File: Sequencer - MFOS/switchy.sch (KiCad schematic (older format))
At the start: 52 parts

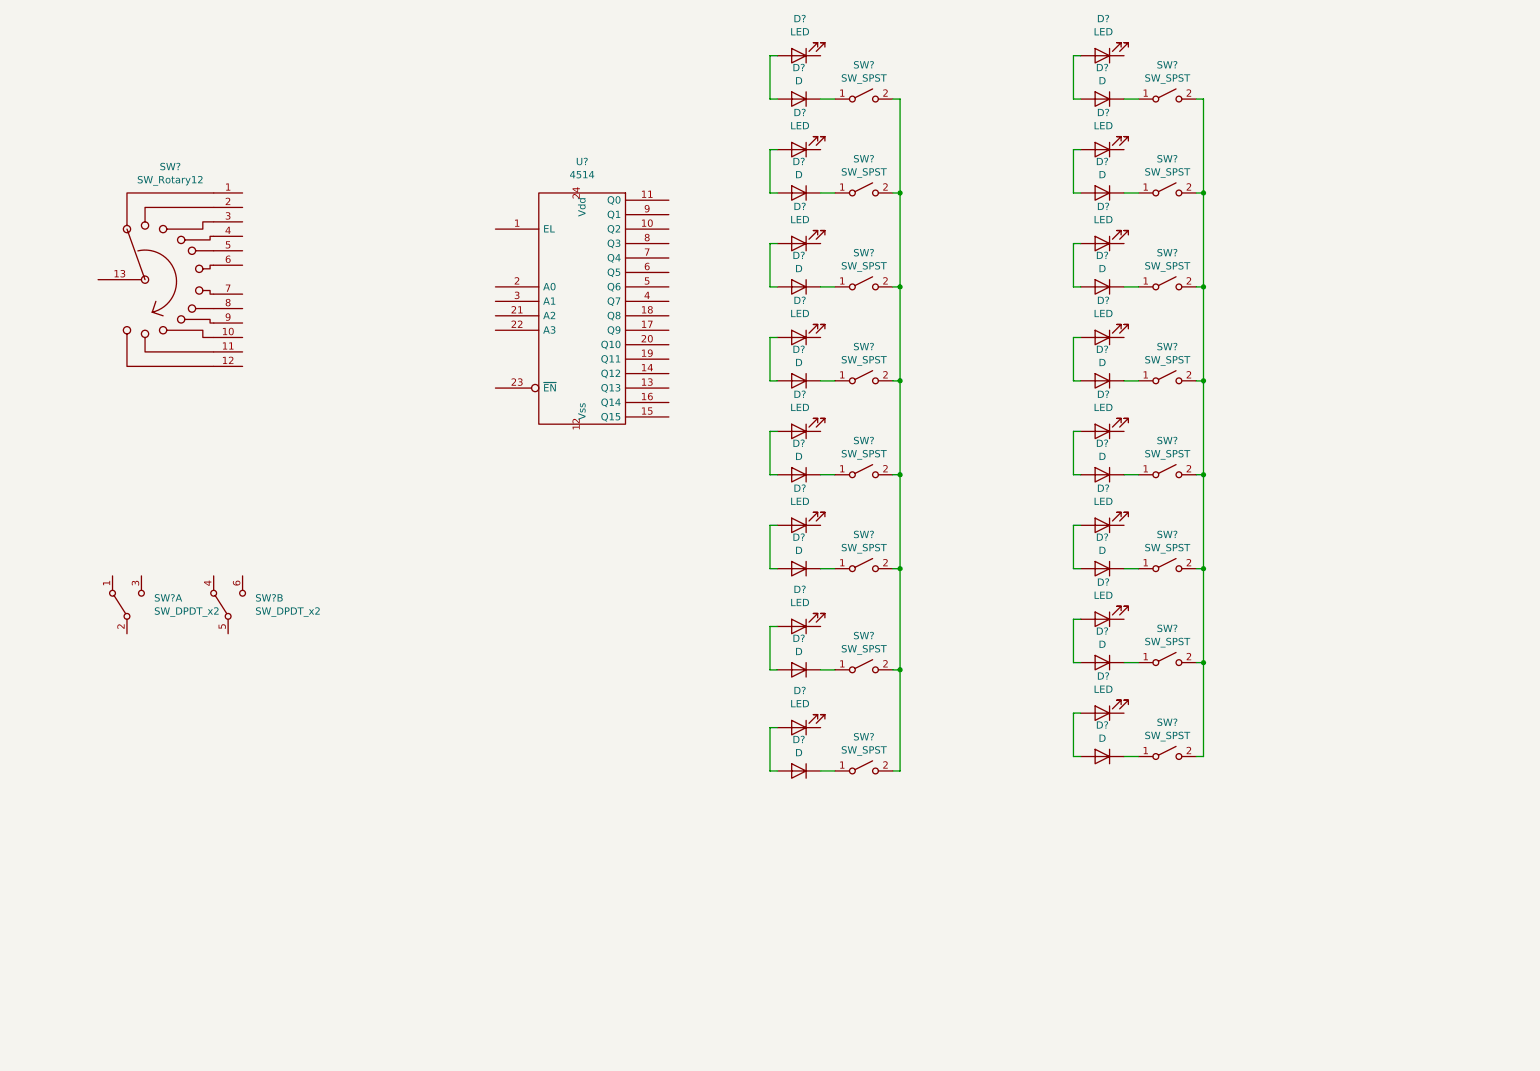
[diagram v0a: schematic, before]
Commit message: finished sequencer schematic
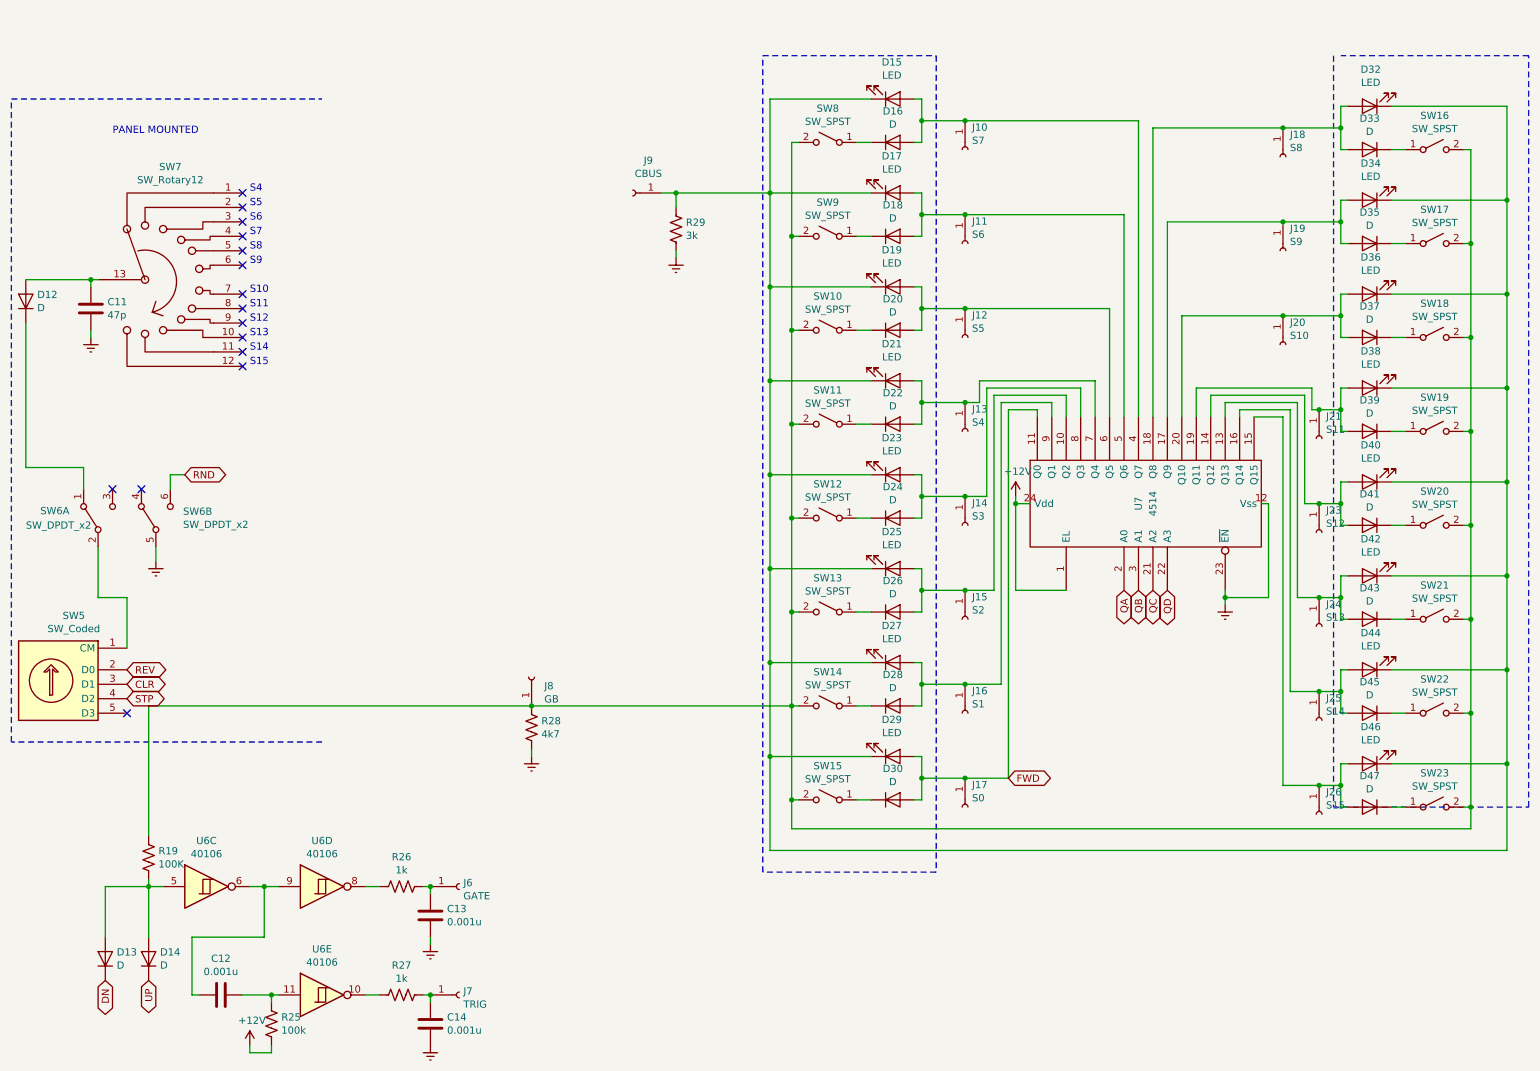
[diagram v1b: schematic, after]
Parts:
- removed D? (x8): LED, symbol Device:LED
- removed D? (x8): D, symbol Device:D
- removed SW? (x8): SW_SPST, symbol Switch:SW_SPST
- added C11: 47p, symbol Device:C
- added C12, C13, C14: 0.001u, symbol Device:C
- added D12, D13, D14, D16, D18, D20, D22, D24, D26, D28, D30: D, symbol Device:D
- added D15, D17, D19, D21, D23, D25, D27, D29: LED, symbol Device:LED
- added J10: S7, symbol Connector:Conn_01x01_Female
- added J11: S6, symbol Connector:Conn_01x01_Female
- added J12: S5, symbol Connector:Conn_01x01_Female
- added J13: S4, symbol Connector:Conn_01x01_Female
- added J14: S3, symbol Connector:Conn_01x01_Female
- added J15: S2, symbol Connector:Conn_01x01_Female
- added J16: S1, symbol Connector:Conn_01x01_Female
- added J17: S0, symbol Connector:Conn_01x01_Female
- added J18: S8, symbol Connector:Conn_01x01_Female
- added J19: S9, symbol Connector:Conn_01x01_Female
- added J20: S10, symbol Connector:Conn_01x01_Female
- added J21: S11, symbol Connector:Conn_01x01_Female
- added J23: S12, symbol Connector:Conn_01x01_Female
- added J24: S13, symbol Connector:Conn_01x01_Female
- added J25: S14, symbol Connector:Conn_01x01_Female
- added J26: S15, symbol Connector:Conn_01x01_Female
- added J6: GATE, symbol Connector:Conn_01x01_Female
- added J7: TRIG, symbol Connector:Conn_01x01_Female
- added J8: GB, symbol Connector:Conn_01x01_Female
- added J9: CBUS, symbol Connector:Conn_01x01_Female
- added R19: 100K, symbol Device:R_US
- added R25: 100k, symbol Device:R_US
- added R26, R27: 1k, symbol Device:R_US
- added R28: 4k7, symbol Device:R_US
- added R29: 3k, symbol Device:R_US
- added SW10, SW11, SW12, SW13, SW14, SW15, SW8, SW9: SW_SPST, symbol Switch:SW_SPST
- added SW5: SW_Coded, symbol Switch:SW_Coded
- added U6: 40106, symbol 4xxx:40106
- gave numbers to parts that had none: 27
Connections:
- net +12V: now reaches U7.1 (EL)
- net +12V: now also U7.24 (Vdd), R25.2
- net at U7.10 (Q2): now also D25.2 (A), D26.2 (A), J15.1 (Pin_1)
- net FWD: now reaches U7.11 (Q0)
- net FWD: now also D29.2 (A), D30.2 (A), J17.1 (Pin_1)
- net Earth: now reaches U7.12 (Vss)
- net Earth: now also SW6.5 (B), U7.23 (~EN), C11.2, C13.2, C14.2, R28.1, R29.1
- net at U7.13 (Q13): now also D42.2 (A), D43.2 (A), J24.1 (Pin_1)
- net at U7.14 (Q12): now also D40.2 (A), D41.2 (A), J23.1 (Pin_1)
- net at U7.15 (Q15): now also D46.2 (A), D47.2 (A), J26.1 (Pin_1)
- net at U7.16 (Q14): now also D44.2 (A), D45.2 (A), J25.1 (Pin_1)
- net at U7.17 (Q9): now also D34.2 (A), D35.2 (A), J19.1 (Pin_1)
- net at U7.18 (Q8): now also D32.2 (A), D33.2 (A), J18.1 (Pin_1)
- net at U7.19 (Q11): now also D38.2 (A), D39.2 (A), J21.1 (Pin_1)
- net QA: now reaches U7.2 (A0)
- net at U7.20 (Q10): now also D36.2 (A), D37.2 (A), J20.1 (Pin_1)
- net QC: now reaches U7.21 (A2)
- net QD: now reaches U7.22 (A3)
- net QB: now reaches U7.3 (A1)
- net at U7.4 (Q7): now also D15.2 (A), D16.2 (A), J10.1 (Pin_1)
- net at U7.5 (Q6): now also D17.2 (A), D18.2 (A), J11.1 (Pin_1)
- net at U7.6 (Q5): now also D19.2 (A), D20.2 (A), J12.1 (Pin_1)
- net at U7.7 (Q4): now also D21.2 (A), D22.2 (A), J13.1 (Pin_1)
- net at U7.8 (Q3): now also D23.2 (A), D24.2 (A), J14.1 (Pin_1)
- net at U7.9 (Q1): now also D27.2 (A), D28.2 (A), J16.1 (Pin_1)
- net at SW7.13: now also C11.1, D12.2 (A)
- net at SW6.1 (A): now also D12.1 (K)
- net at SW6.2 (B): now also SW5.1 (CM)
- net RND: now reaches SW6.6 (C)
- net at D32.1 (K): now also D34.1 (K), D36.1 (K), D38.1 (K), D40.1 (K), D42.1 (K), D44.1 (K), D46.1 (K), D15.1 (K), D17.1 (K), D19.1 (K), D21.1 (K), D23.1 (K), D25.1 (K), D27.1 (K), D29.1 (K), J9.1 (Pin_1), R29.2
- net at SW16.2 (B), SW17.2 (B), SW18.2 (B)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: now also J8.1 (Pin_1), R19.1, R28.2, SW10.2 (B), SW11.2 (B), SW12.2 (B), SW13.2 (B), SW14.2 (B), SW15.2 (B), SW8.2 (B), SW9.2 (B)
- new net: D13.2 (A), D14.2 (A), R19.2, U6.5
- new net: C12.2, U6.6, U6.9
- new net: R26.2, U6.8
- new net: R27.2, U6.10
- new net: C12.1, R25.1, U6.11
- new net: C14.1, J7.1 (Pin_1), R27.1
- new net: C13.1, J6.1 (Pin_1), R26.1
- new net: D16.1 (K), SW8.1 (A)
- new net: D18.1 (K), SW9.1 (A)
- new net: D20.1 (K), SW10.1 (A)
- new net: D22.1 (K), SW11.1 (A)
- new net: D24.1 (K), SW12.1 (A)
- new net: D26.1 (K), SW13.1 (A)
- new net: D28.1 (K), SW14.1 (A)
- new net: D30.1 (K), SW15.1 (A)
- new net CLR: SW5.3 (D1)
- new net DN: D13.1 (K)
- new net REV: SW5.2 (D0)
- new net STP: SW5.4 (D2)
- new net UP: D14.1 (K)
- no-connect marks 0 -> 15
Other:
- note added: "PANEL MOUNTED"
- note added: "S10"
- note added: "S11"
- note added: "S12"
- note added: "S13"
- note added: "S14"
- note added: "S15"
- note added: "S4"
- note added: "S5\n"
- note added: "S6"
- note added: "S7"
- note added: "S8"
- note added: "S9"
- moved on the sheet: D32, D33, D34, D35, D36, D37, D38, D39, D40, D41, D42, D43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

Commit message: sequencer pcb designed and base silkscreen
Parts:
- C11, C12, C13, C14: footprint (none) -> Capacitor_THT:C_Rect_L7.0mm_W2.5mm_P5.00mm
- D12, D13, D14: footprint (none) -> Diode_THT:D_T-1_P5.08mm_Horizontal
- J10, J11, J12, J13, J14, J15, J16, J17, J18, J19, J20, J21, J23, J24, J25, J26, J6, J7, J8, J9: footprint (none) -> Connector_Wire:SolderWirePad_1x01_Drill1mm
- R19, R25, R26, R27, R28, R29: footprint (none) -> Resistor_THT:R_Axial_DIN0207_L6.3mm_D2.5mm_P7.62mm_Horizontal
- U6: footprint (none) -> Package_DIP:DIP-14_W7.62mm_Socket
- U7: footprint (none) -> Package_SO:SOIC-24W_7.5x15.4mm_P1.27mm
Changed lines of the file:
@@
 F 0 "U7" H 8350 3750 50  0000 C CNN
 F 1 "4514" H 8350 3650 50  0000 C CNN
-F 2 "" H 8350 3700 50  0001 C CNN
+F 2 "Package_SO:SOIC-24W_7.5x15.4mm_P1.27mm" H 8350 3700 50  0001 C CNN
 F 3 "" H 8350 3700 50  0001 C CNN
 	1    8350 3700
@@
 F 0 "D12" V 646 2221 50  0000 R CNN
 F 1 "D" V 555 2221 50  0000 R CNN
-F 2 "" H 600 2300 50  0001 C CNN
+F 2 "Diode_THT:D_T-1_P5.08mm_Horizontal" H 600 2300 50  0001 C CNN
 F 3 "~" H 600 2300 50  0001 C CNN
 	1    600  2300
@@
 F 0 "C11" H 1165 2396 50  0000 L CNN
 F 1 "47p" H 1165 2305 50  0000 L CNN
-F 2 "" H 1088 2200 50  0001 C CNN
+F 2 "Capacitor_THT:C_Rect_L7.0mm_W2.5mm_P5.00mm" H 1088 2200 50  0001 C CNN
 F 3 "~" H 1050 2350 50  0001 C CNN
 	1    1050 2350
@@
 F 0 "U6" H 1850 6667 50  0000 C CNN
 F 1 "40106" H 1850 6576 50  0000 C CNN
-F 2 "" H 1850 6350 50  0001 C CNN
+F 2 "Package_DIP:DIP-14_W7.62mm_Socket" H 1850 6350 50  0001 C CNN
 F 3 "https://assets.nexperia.com/documents/data-sheet/HEF40106B.pdf" H 1850 6350 50  0001 C CNN
 	3    1850 6350
@@
 F 0 "U6" H 2650 6667 50  0000 C CNN
 F 1 "40106" H 2650 6576 50  0000 C CNN
-F 2 "" H 2650 6350 50  0001 C CNN
+F 2 "Package_DIP:DIP-14_W7.62mm_Socket" H 2650 6350 50  0001 C CNN
 F 3 "https://assets.nexperia.com/documents/data-sheet/HEF40106B.pdf" H 2650 6350 50  0001 C CNN
 	4    2650 6350
@@
 F 0 "U6" H 2650 7417 50  0000 C CNN
 F 1 "40106" H 2650 7326 50  0000 C CNN
-F 2 "" H 2650 7100 50  0001 C CNN
+F 2 "Package_DIP:DIP-14_W7.62mm_Socket" H 2650 7100 50  0001 C CNN
 F 3 "https://assets.nexperia.com/documents/data-sheet/HEF40106B.pdf" H 2650 7100 50  0001 C CNN
 	5    2650 7100
@@
 F 0 "D13" V 1196 6771 50  0000 R CNN
 F 1 "D" V 1105 6771 50  0000 R CNN
-F 2 "" H 1150 6850 50  0001 C CNN
+F 2 "Diode_THT:D_T-1_P5.08mm_Horizontal" H 1150 6850 50  0001 C CNN
 F 3 "~" H 1150 6850 50  0001 C CNN
 	1    1150 6850
@@
 F 0 "D14" V 1496 6771 50  0000 R CNN
 F 1 "D" V 1405 6771 50  0000 R CNN
-F 2 "" H 1450 6850 50  0001 C CNN
+F 2 "Diode_THT:D_T-1_P5.08mm_Horizontal" H 1450 6850 50  0001 C CNN
 F 3 "~" H 1450 6850 50  0001 C CNN
 	1    1450 6850
@@
 F 0 "C12" V 1698 7100 50  0000 C CNN
 F 1 "0.001u" V 1789 7100 50  0000 C CNN
-F 2 "" H 1988 6950 50  0001 C CNN
+F 2 "Capacitor_THT:C_Rect_L7.0mm_W2.5mm_P5.00mm" H 1988 6950 50  0001 C CNN
 F 3 "~" H 1950 7100 50  0001 C CNN
 	1    1950 7100
@@
 F 0 "R19" H 1518 6196 50  0000 L CNN
 F 1 "100K" H 1518 6105 50  0000 L CNN
-F 2 "" V 1490 6140 50  0001 C CNN
+F 2 "Resistor_THT:R_Axial_DIN0207_L6.3mm_D2.5mm_P7.62mm_Horizontal" V 1490 6140 50  0001 C CNN
 F 3 "~" H 1450 6150 50  0001 C CNN
 	1    1450 6150
@@
 F 0 "R25" H 2368 7346 50  0000 L CNN
 F 1 "100k" H 2368 7255 50  0000 L CNN
-F 2 "" V 2340 7290 50  0001 C CNN
+F 2 "Resistor_THT:R_Axial_DIN0207_L6.3mm_D2.5mm_P7.62mm_Horizontal" V 2340 7290 50  0001 C CNN
 F 3 "~" H 2300 7300 50  0001 C CNN
 	1    2300 7300
@@
 F 0 "R27" V 2995 7100 50  0000 C CNN
 F 1 "1k" V 3086 7100 50  0000 C CNN
-F 2 "" V 3240 7090 50  0001 C CNN
+F 2 "Resistor_THT:R_Axial_DIN0207_L6.3mm_D2.5mm_P7.62mm_Horizontal" V 3240 7090 50  0001 C CNN
 F 3 "~" H 3200 7100 50  0001 C CNN
 	1    3200 7100
@@
 F 0 "R26" V 2995 6350 50  0000 C CNN
 F 1 "1k" V 3086 6350 50  0000 C CNN
-F 2 "" V 3240 6340 50  0001 C CNN
+F 2 "Resistor_THT:R_Axial_DIN0207_L6.3mm_D2.5mm_P7.62mm_Horizontal" V 3240 6340 50  0001 C CNN
 F 3 "~" H 3200 6350 50  0001 C CNN
 	1    3200 6350
@@
 F 0 "C13" H 3515 6596 50  0000 L CNN
 F 1 "0.001u" H 3515 6505 50  0000 L CNN
-F 2 "" H 3438 6400 50  0001 C CNN
+F 2 "Capacitor_THT:C_Rect_L7.0mm_W2.5mm_P5.00mm" H 3438 6400 50  0001 C CNN
 F 3 "~" H 3400 6550 50  0001 C CNN
 	1    3400 6550
@@
 F 0 "C14" H 3515 7346 50  0000 L CNN
 F 1 "0.001u" H 3515 7255 50  0000 L CNN
-F 2 "" H 3438 7150 50  0001 C CNN
+F 2 "Capacitor_THT:C_Rect_L7.0mm_W2.5mm_P5.00mm" H 3438 7150 50  0001 C CNN
 F 3 "~" H 3400 7300 50  0001 C CNN
 	1    3400 7300
@@
 F 0 "R29" H 5032 1754 50  0000 R CNN
 F 1 "3k" H 5032 1845 50  0000 R CNN
-F 2 "" V 5140 1790 50  0001 C CNN
+F 2 "Resistor_THT:R_Axial_DIN0207_L6.3mm_D2.5mm_P7.62mm_Horizontal" V 5140 1790 50  0001 C CNN
 F 3 "~" H 5100 1800 50  0001 C CNN
 	1    5100 1800
@@
 F 0 "J9" H 4692 1325 50  0000 C CNN
 F 1 "CBUS" H 4692 1416 50  0000 C CNN
-F 2 "" H 4800 1550 50  0001 C CNN
+F 2 "Connector_Wire:SolderWirePad_1x01_Drill1mm" H 4800 1550 50  0001 C CNN
 F 3 "~" H 4800 1550 50  0001 C CNN
 	1    4800 1550
@@
 F 0 "R28" H 4032 5204 50  0000 R CNN
 F 1 "4k7" H 4032 5295 50  0000 R CNN
-F 2 "" V 4140 5240 50  0001 C CNN
+F 2 "Resistor_THT:R_Axial_DIN0207_L6.3mm_D2.5mm_P7.62mm_Horizontal" V 4140 5240 50  0001 C CNN
 F 3 "~" H 4100 5250 50  0001 C CNN
 	1    4100 5250
@@
 F 0 "J8" V 4038 4812 50  0000 R CNN
 F 1 "GB" V 3947 4812 50  0000 R CNN
-F 2 "" H 4100 4900 50  0001 C CNN
+F 2 "Connector_Wire:SolderWirePad_1x01_Drill1mm" H 4100 4900 50  0001 C CNN
 F 3 "~" H 4100 4900 50  0001 C CNN
 	1    4100 4900
@@
 F 0 "J6" H 3628 6376 50  0000 L CNN
 F 1 "GATE" H 3628 6285 50  0000 L CNN
-F 2 "" H 3600 6350 50  0001 C CNN
+F 2 "Connector_Wire:SolderWirePad_1x01_Drill1mm" H 3600 6350 50  0001 C CNN
 F 3 "~" H 3600 6350 50  0001 C CNN
 	1    3600 6350
@@
 F 0 "J7" H 3628 7126 50  0000 L CNN
 F 1 "TRIG" H 3628 7035 50  0000 L CNN
-F 2 "" H 3600 7100 50  0001 C CNN
+F 2 "Connector_Wire:SolderWirePad_1x01_Drill1mm" H 3600 7100 50  0001 C CNN
 F 3 "~" H 3600 7100 50  0001 C CNN
 	1    3600 7100
@@
 F 0 "J17" V 6946 5848 50  0000 L CNN
 F 1 "S0" V 7037 5848 50  0000 L CNN
-F 2 "" H 7100 5800 50  0001 C CNN
+F 2 "Connector_Wire:SolderWirePad_1x01_Drill1mm" H 7100 5800 50  0001 C CNN
 F 3 "~" H 7100 5800 50  0001 C CNN
 	1    7100 5800
@@
 F 0 "J16" V 6946 5198 50  0000 L CNN
 F 1 "S1" V 7037 5198 50  0000 L CNN
-F 2 "" H 7100 5150 50  0001 C CNN
+F 2 "Connector_Wire:SolderWirePad_1x01_Drill1mm" H 7100 5150 50  0001 C CNN
 F 3 "~" H 7100 5150 50  0001 C CNN
 	1    7100 5150
@@
 F 0 "J15" V 6946 4548 50  0000 L CNN
 F 1 "S2" V 7037 4548 50  0000 L CNN
-F 2 "" H 7100 4500 50  0001 C CNN
+F 2 "Connector_Wire:SolderWirePad_1x01_Drill1mm" H 7100 4500 50  0001 C CNN
 F 3 "~" H 7100 4500 50  0001 C CNN
 	1    7100 4500
@@
 F 0 "J14" V 6946 3898 50  0000 L CNN
 F 1 "S3" V 7037 3898 50  0000 L CNN
-F 2 "" H 7100 3850 50  0001 C CNN
+F 2 "Connector_Wire:SolderWirePad_1x01_Drill1mm" H 7100 3850 50  0001 C CNN
 F 3 "~" H 7100 3850 50  0001 C CNN
 	1    7100 3850
@@
 F 0 "J13" V 6946 3248 50  0000 L CNN
 F 1 "S4" V 7037 3248 50  0000 L CNN
-F 2 "" H 7100 3200 50  0001 C CNN
+F 2 "Connector_Wire:SolderWirePad_1x01_Drill1mm" H 7100 3200 50  0001 C CNN
 F 3 "~" H 7100 3200 50  0001 C CNN
 	1    7100 3200
@@
 F 0 "J12" V 6946 2598 50  0000 L CNN
 F 1 "S5" V 7037 2598 50  0000 L CNN
-F 2 "" H 7100 2550 50  0001 C CNN
+F 2 "Connector_Wire:SolderWirePad_1x01_Drill1mm" H 7100 2550 50  0001 C CNN
 F 3 "~" H 7100 2550 50  0001 C CNN
 	1    7100 2550
@@
 F 0 "J11" V 6946 1948 50  0000 L CNN
 F 1 "S6" V 7037 1948 50  0000 L CNN
-F 2 "" H 7100 1900 50  0001 C CNN
+F 2 "Connector_Wire:SolderWirePad_1x01_Drill1mm" H 7100 1900 50  0001 C CNN
 F 3 "~" H 7100 1900 50  0001 C CNN
 	1    7100 1900
@@
 F 0 "J10" V 6946 1298 50  0000 L CNN
 F 1 "S7" V 7037 1298 50  0000 L CNN
-F 2 "" H 7100 1250 50  0001 C CNN
+F 2 "Connector_Wire:SolderWirePad_1x01_Drill1mm" H 7100 1250 50  0001 C CNN
 F 3 "~" H 7100 1250 50  0001 C CNN
 	1    7100 1250
@@
 F 0 "J18" V 9146 1348 50  0000 L CNN
 F 1 "S8" V 9237 1348 50  0000 L CNN
-F 2 "" H 9300 1300 50  0001 C CNN
+F 2 "Connector_Wire:SolderWirePad_1x01_Drill1mm" H 9300 1300 50  0001 C CNN
 F 3 "~" H 9300 1300 50  0001 C CNN
 	1    9300 1300
@@
 F 0 "J19" V 9146 1998 50  0000 L CNN
 F 1 "S9" V 9237 1998 50  0000 L CNN
-F 2 "" H 9300 1950 50  0001 C CNN
+F 2 "Connector_Wire:SolderWirePad_1x01_Drill1mm" H 9300 1950 50  0001 C CNN
 F 3 "~" H 9300 1950 50  0001 C CNN
 	1    9300 1950
@@
 F 0 "J20" V 9146 2648 50  0000 L CNN
 F 1 "S10" V 9237 2648 50  0000 L CNN
-F 2 "" H 9300 2600 50  0001 C CNN
+F 2 "Connector_Wire:SolderWirePad_1x01_Drill1mm" H 9300 2600 50  0001 C CNN
 F 3 "~" H 9300 2600 50  0001 C CNN
 	1    9300 2600
@@
 F 0 "J21" V 9396 3298 50  0000 L CNN
 F 1 "S11" V 9487 3298 50  0000 L CNN
-F 2 "" H 9550 3250 50  0001 C CNN
+F 2 "Connector_Wire:SolderWirePad_1x01_Drill1mm" H 9550 3250 50  0001 C CNN
 F 3 "~" H 9550 3250 50  0001 C CNN
 	1    9550 3250
@@
 F 0 "J23" V 9396 3948 50  0000 L CNN
 F 1 "S12" V 9487 3948 50  0000 L CNN
-F 2 "" H 9550 3900 50  0001 C CNN
+F 2 "Connector_Wire:SolderWirePad_1x01_Drill1mm" H 9550 3900 50  0001 C CNN
 F 3 "~" H 9550 3900 50  0001 C CNN
 	1    9550 3900
@@
 F 0 "J24" V 9396 4598 50  0000 L CNN
 F 1 "S13" V 9487 4598 50  0000 L CNN
-F 2 "" H 9550 4550 50  0001 C CNN
+F 2 "Connector_Wire:SolderWirePad_1x01_Drill1mm" H 9550 4550 50  0001 C CNN
 F 3 "~" H 9550 4550 50  0001 C CNN
 	1    9550 4550
@@
 F 0 "J25" V 9396 5248 50  0000 L CNN
 F 1 "S14" V 9487 5248 50  0000 L CNN
-F 2 "" H 9550 5200 50  0001 C CNN
+F 2 "Connector_Wire:SolderWirePad_1x01_Drill1mm" H 9550 5200 50  0001 C CNN
 F 3 "~" H 9550 5200 50  0001 C CNN
 	1    9550 5200
@@
 F 0 "J26" V 9396 5898 50  0000 L CNN
 F 1 "S15" V 9487 5898 50  0000 L CNN
-F 2 "" H 9550 5850 50  0001 C CNN
+F 2 "Connector_Wire:SolderWirePad_1x01_Drill1mm" H 9550 5850 50  0001 C CNN
 F 3 "~" H 9550 5850 50  0001 C CNN
 	1    9550 5850
